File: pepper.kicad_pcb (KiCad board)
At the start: 2 copper layers, 73 x 47 mm, 50 parts, among them J1 USB, J2 Debug, J3 Conn_01x06, Q1 BSS138, SW1 Reset, SW2 Boot, SW3 Action, SW4 Action, U1 ESP32-S3-WROOM-1, U2 AP2112K-3.3

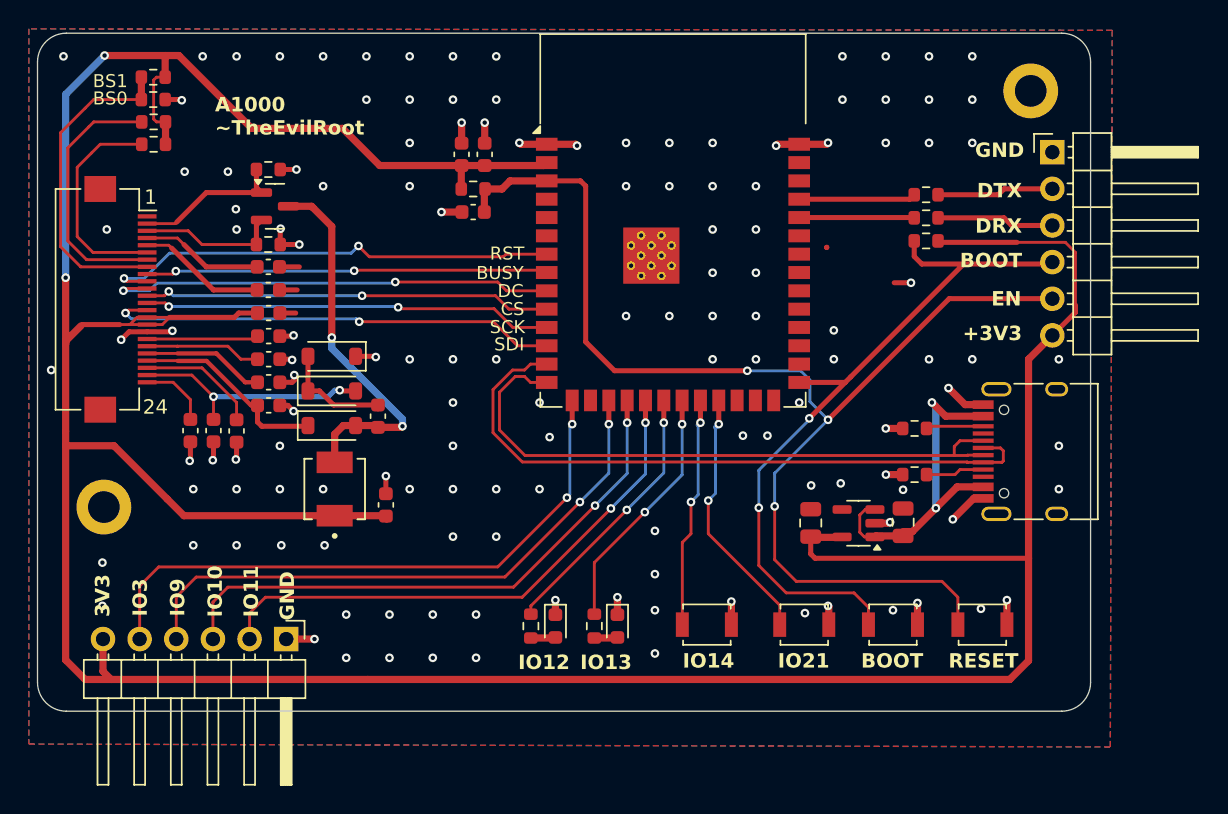
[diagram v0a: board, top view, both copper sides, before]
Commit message: 4 layer board. Battery charger
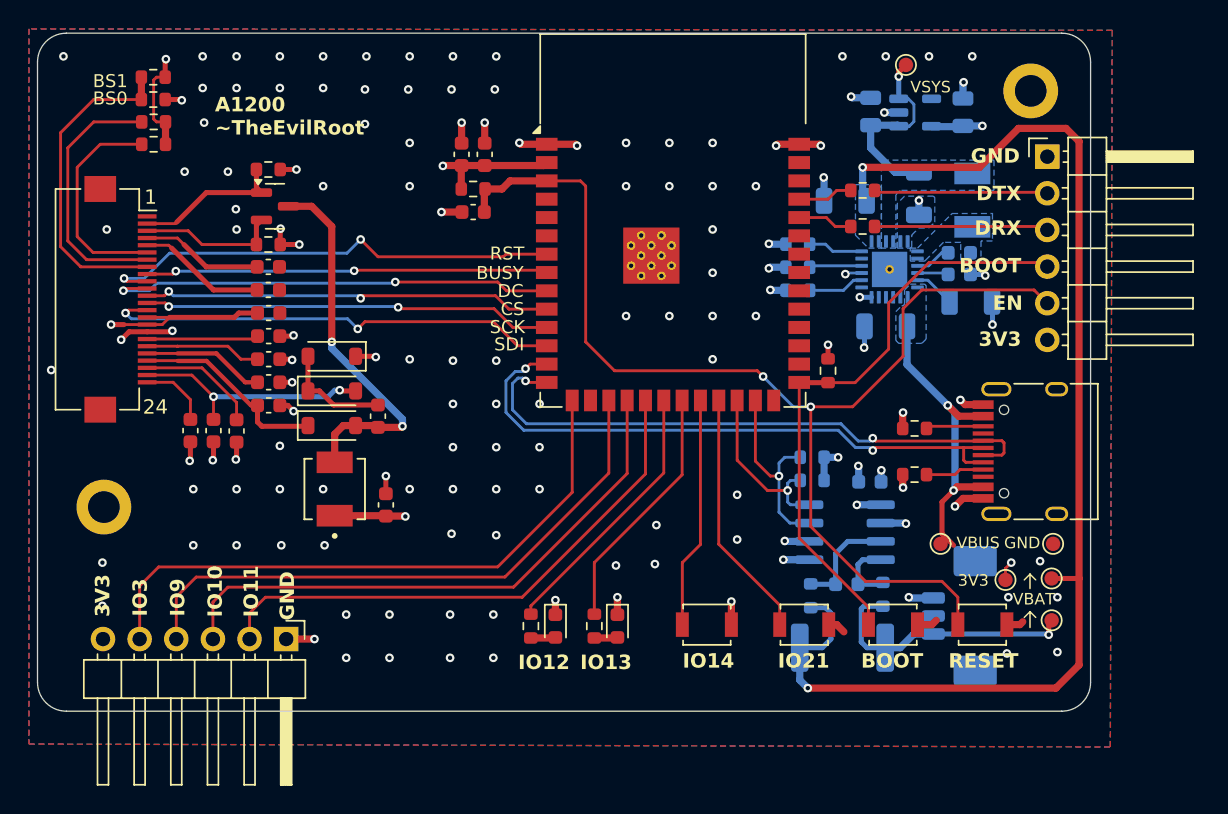
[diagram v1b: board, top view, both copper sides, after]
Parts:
- added C12: 1u, Capacitor_SMD:C_1206_3216Metric, B.Cu at (192.6, 96.7)
- added C19: 10u, Capacitor_SMD:C_1206_3216Metric, B.Cu at (189.8, 88.0)
- added C20: 10u, Capacitor_SMD:C_1206_3216Metric, B.Cu at (194.9, 87.5)
- added C21: 47n, Capacitor_SMD:C_0603_1608Metric, B.Cu at (197.7, 91.6)
- added C22: 10u, Capacitor_SMD:C_1206_3216Metric, B.Cu at (198.5, 95.0)
- added C23: 4u7, Capacitor_SMD:C_0603_1608Metric, B.Cu at (197.7, 93.1)
- added C24: 100n, Capacitor_SMD:C_0603_1608Metric, B.Cu at (189.9, 114.6)
- added C25: 100n, Capacitor_SMD:C_0603_1608Metric, B.Cu at (191.5, 107.5)
- added J4: Conn_01x03, Connector_Molex:Molex_PicoBlade_53261-0371_1x03-1MP_P1.25mm_Horizontal, B.Cu at (198.3, 116.8)
- added L2: 1u, Library:IND_CSAB0420-2R2M, B.Cu at (198.6, 88.0)
- added R15: 450R, Resistor_SMD:R_0603_1608Metric, B.Cu at (186.5, 92.6)
- added R16: 240R, Resistor_SMD:R_0603_1608Metric, B.Cu at (186.5, 94.2)
- added R17: 0, Resistor_SMD:R_0603_1608Metric, B.Cu at (186.5, 91.0)
- added R18: R025, Resistor_SMD:R_2512_6332Metric, B.Cu at (189.6, 119.0)
- added R19: 10R, Resistor_SMD:R_0603_1608Metric, B.Cu at (192.4, 115.3)
- added R20: 10R, Resistor_SMD:R_0603_1608Metric, B.Cu at (187.4, 115.4)
- added R21: 2k7, Resistor_SMD:R_0603_1608Metric, B.Cu at (187.5, 105.8)
- added R22: 2k7, Resistor_SMD:R_0603_1608Metric, B.Cu at (187.5, 107.4)
- added TP1: 3V3, TestPoint:TestPoint_Pad_D1.0mm, F.Cu at (200.9, 114.3)
- added TP2: VBUS, TestPoint:TestPoint_Pad_D1.0mm, F.Cu at (196.4, 111.8)
- added TP3: VBAT, TestPoint:TestPoint_Pad_D1.0mm, F.Cu at (204.1, 114.2)
- added TP4: GND, TestPoint:TestPoint_Pad_D1.0mm, F.Cu at (204.2, 111.8)
- added TP5: VBAT_IN, TestPoint:TestPoint_Pad_D1.0mm, F.Cu at (204.1, 117.1)
- added TP6: VSYS, TestPoint:TestPoint_Pad_D1.0mm, F.Cu at (194.0, 78.6)
- added U4: BQ25606RGER, Library:QFN50P400X400X100-25N, B.Cu at (192.9, 92.8)
- added U5: INA219AxD, Package_SO:SOIC-8_3.9x4.9mm_P1.27mm, B.Cu at (189.8, 111.0)
- C1, C2, U2: moved to B.Cu
- J3: value Conn_01x06 -> Breakout
- moved C2 30.4 mm to (198.0, 81.9)
- moved U2 28.7 mm to (194.6, 81.9), turned to 0 degrees
- moved C1 28.6 mm to (191.6, 81.8)
- moved R2 11.3 mm to (188.6, 99.8), turned to -90 degrees
- moved R12 4.44 mm to (191.0, 89.8)
- moved R11 4.41 mm to (191.0, 87.3)
- moved J2 0.47 mm to (203.8, 85.0)
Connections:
- C1 pad 1: +5V -> VSYS
- J1 pad A4: +5V -> VBUS
- J1 pad A9: +5V -> VBUS
- J1 pad B4: +5V -> VBUS
- J1 pad B9: +5V -> VBUS
- U1 pad 24: unconnected-(U1-IO47-Pad24) -> METER_SCL
- U1 pad 25: unconnected-(U1-IO48-Pad25) -> METER_SDA
- U2 pad 1: +5V -> VSYS
- U2 pad 3: +5V -> VSYS
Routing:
- net +3V3: track 257.3 -> 43.6 mm, vias 2 -> 10
- net VBAT: track 0.00 -> 85.0 mm, vias 0 -> 2
- net +5V: track 23.8 -> 0.00 mm, vias 2 -> 0
- net VBUS: track 0.00 -> 22.2 mm, vias 0 -> 2
- net VBAT_IN: track 0.00 -> 18.0 mm, vias 0 -> 1
- net GND: track 55.7 -> 69.8 mm, vias 137 -> 138
- net VSYS: track 0.00 -> 13.7 mm, vias 0 -> 1
- net METER_SDA: track 0.00 -> 13.7 mm, vias 0 -> 1
- net METER_SCL: track 0.00 -> 12.3 mm, vias 0 -> 1
- net /ESP_BOOT: track 51.0 -> 41.0 mm, vias 2 -> 0
- net /Battery/METER_IN-: track 0.00 -> 7.30 mm
- net /Battery/METER_IN+: track 0.00 -> 4.68 mm
- net /ESP_TX: track 8.10 -> 3.83 mm
- net /ESP_RX: track 7.98 -> 3.83 mm
- net /ESP_EN: track 85.6 -> 81.7 mm, vias 3 -> 2
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- added copper zone on In1.Cu, net +3V3
- added copper zone on B.Cu, net /Battery/PMIC_SW
- added copper zone on In2.Cu, net GND
- added copper zone on B.Cu, net VBAT
- added copper zone on B.Cu, net VBUS
- added copper zone on B.Cu, net VSYS
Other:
- copper layers 2 -> 4
- board text added: "A1200 ~TheEvilRoot"
- board text added: "VBAT"
- board text added: "VBUS"
- board text added: "VSYS"
- board text removed: "+3V3"
- board text removed: "A1000 ~TheEvilRoot"
